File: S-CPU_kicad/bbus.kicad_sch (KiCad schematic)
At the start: 49 parts

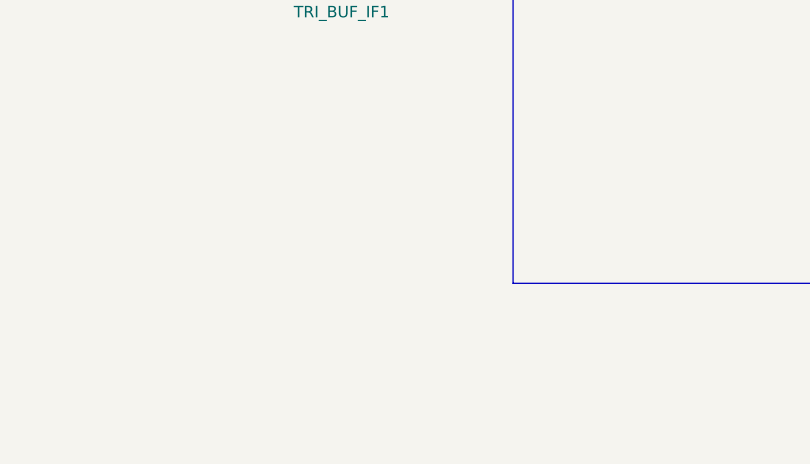
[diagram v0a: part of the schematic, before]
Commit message: Fix ERC errors in schematics.
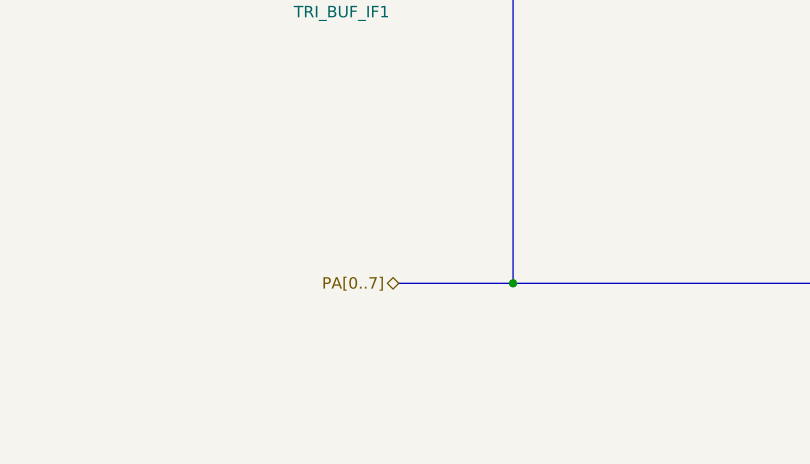
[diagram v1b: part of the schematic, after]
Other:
- company: (none) -> Author: Regis Galland
- title: (none) -> Reverse Engineered SNES S-CPU Schematics 
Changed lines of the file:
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@@
 (kicad_sch (version 20230121) (generator eeschema)
   (paper "A3")
+  (title_block
+    (title "Reverse Engineered SNES S-CPU Schematics ")
+    (date "2023-10-21")
+    (rev "0.1")
+    (company "Author: Regis Galland")
+  )
   (junction (at 292.1 222.25) (diameter 0) (color 0 0 0 0)
   )
@@
   (junction (at 181.61 124.46) (diameter 0) (color 0 0 0 0)
   )
+  (junction (at 120.65 222.25) (diameter 0) (color 0 0 0 0)
+  )
   (junction (at 264.16 124.46) (diameter 0) (color 0 0 0 0)
   )
@@
   )
   (wire (pts (xy 165.1 77.47) (xy 184.15 77.47))
+    (stroke (width 0) (type default))
+  )
+  (bus (pts (xy 107.95 222.25) (xy 120.65 222.25))
     (stroke (width 0) (type default))
   )
@@
     (effects (font (size 1.27 1.27)) (justify right))
   )
+  (hierarchical_label "PA[0..7]" (shape tri_state) (at 107.95 222.25 180) (fields_autoplaced)
+    (effects (font (size 1.27 1.27)) (justify right))
+  )

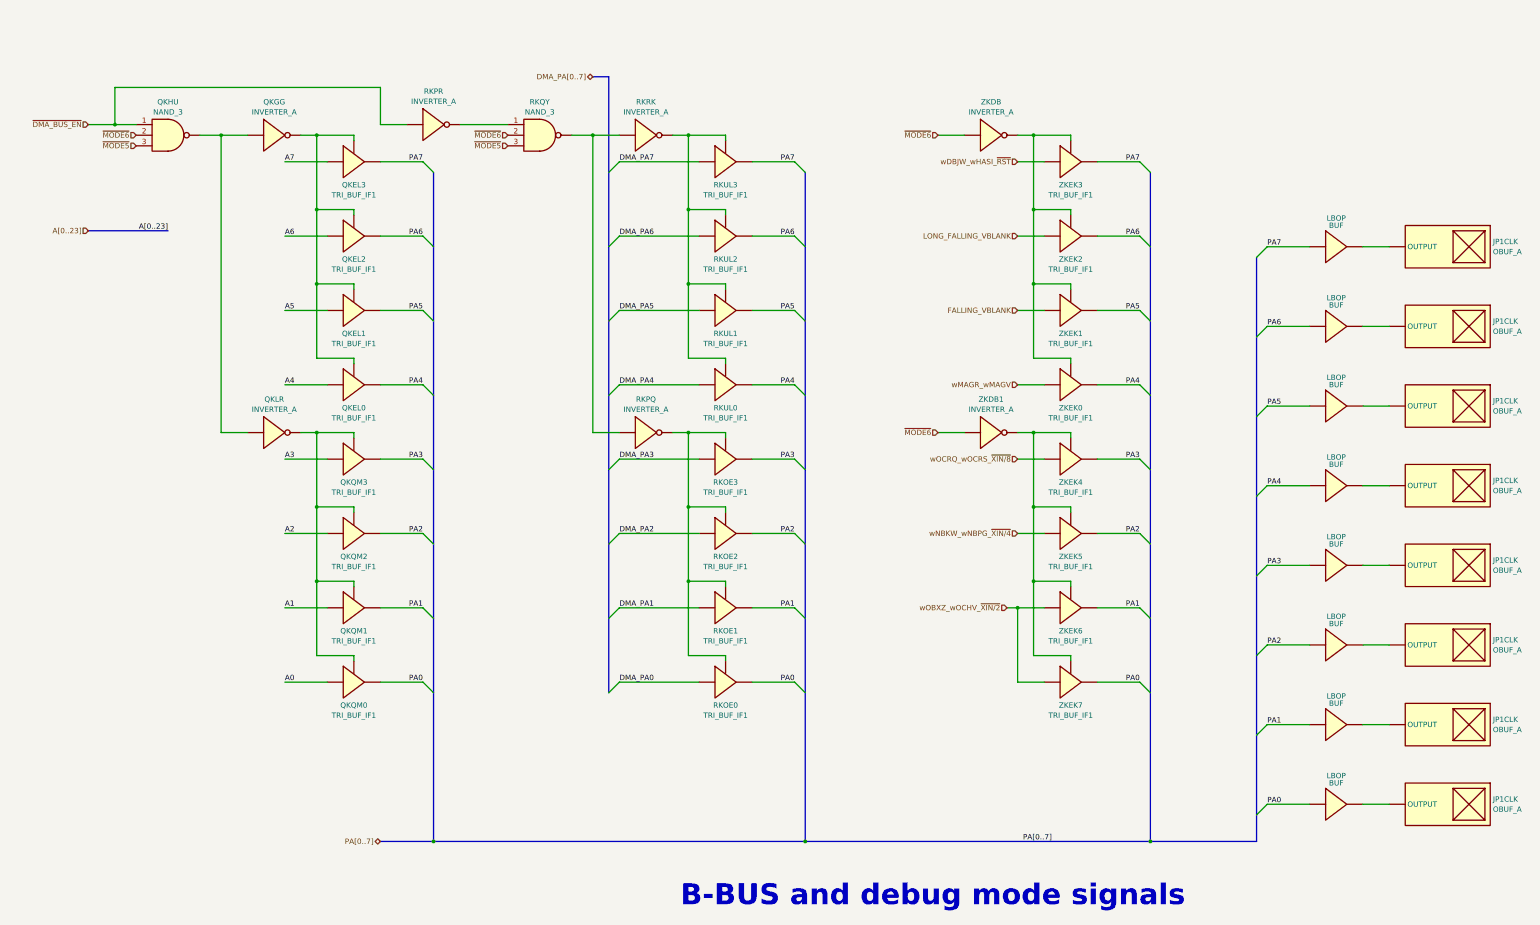
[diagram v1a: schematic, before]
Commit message: Big rework on the hierachical sheet to make thigs a bit clearer. PDF exported for Rev 0.1.
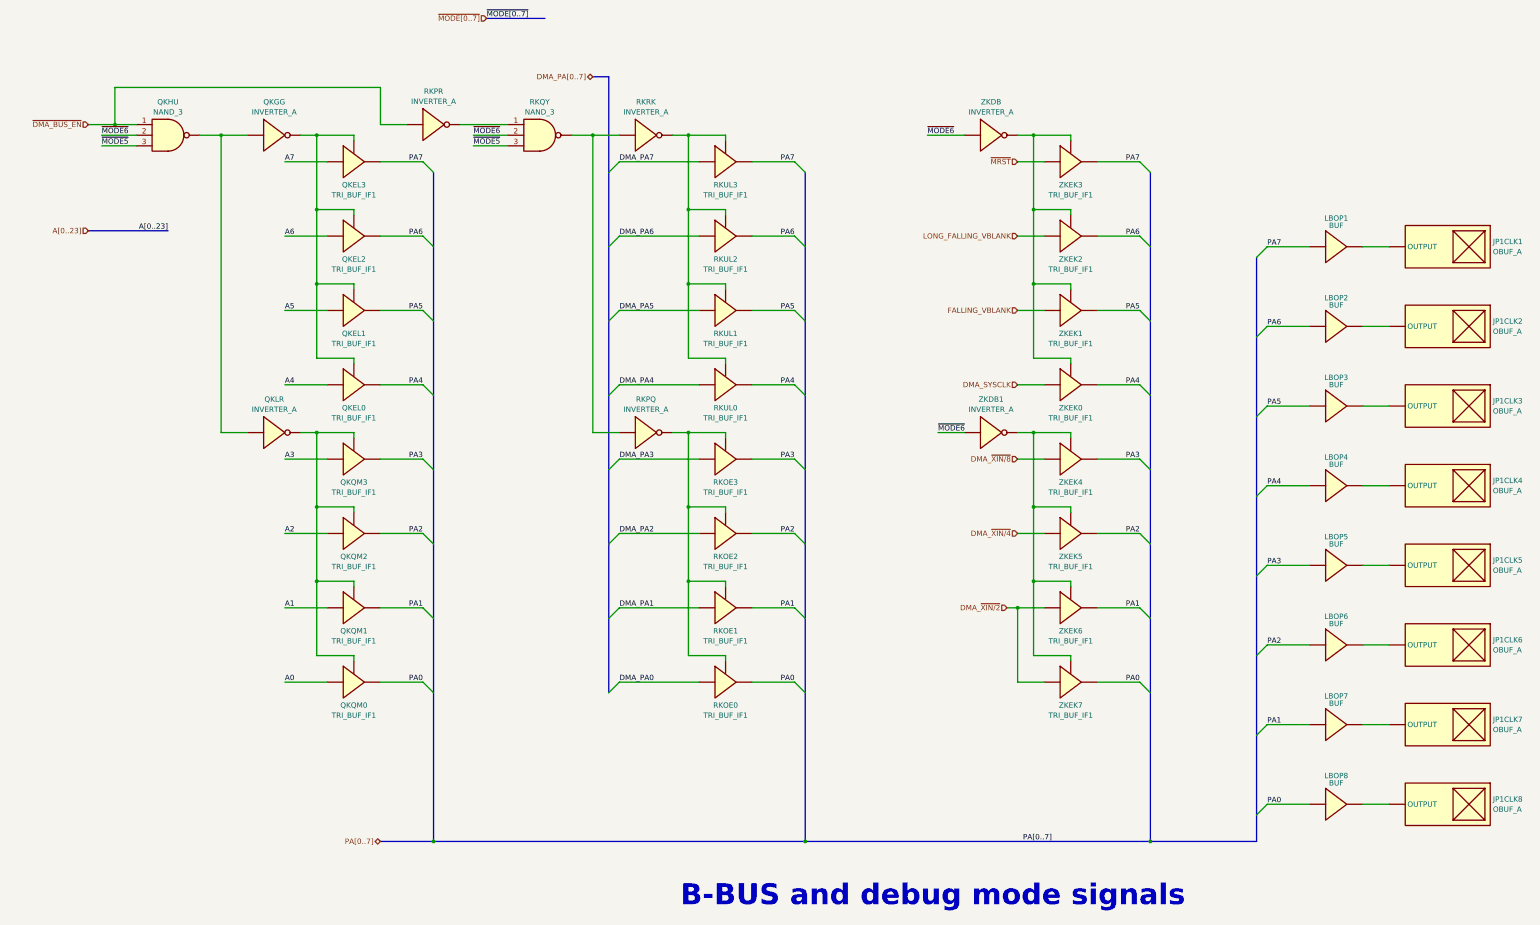
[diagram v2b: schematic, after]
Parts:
- renumbered JP1CLK to JP1CLK1, JP1CLK to JP1CLK2, JP1CLK to JP1CLK3, JP1CLK to JP1CLK4, JP1CLK to JP1CLK5, JP1CLK to JP1CLK6, JP1CLK to JP1CLK7, JP1CLK to JP1CLK8, LBOP to LBOP1, LBOP to LBOP2, LBOP to LBOP3, LBOP to LBOP4, LBOP to LBOP5, LBOP to LBOP6, LBOP to LBOP7, LBOP to LBOP8
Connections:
- net wDBJW_wHASI_~{RST} renamed ~{MRST}
- net wMAGR_wMAGV renamed DMA_SYSCLK
- net wNBKW_wNBPG_~{XIN/4} renamed DMA_~{XIN/4}
- net wOBXZ_wOCHV_~{XIN/2} renamed DMA_~{XIN/2}
- net wOCRQ_wOCRS_~{XIN/8} renamed DMA_~{XIN/8}
